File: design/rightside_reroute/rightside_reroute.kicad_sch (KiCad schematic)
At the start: 191 parts, among them IC2 XC9148G50CER-G, IC3 nRF52833-QDAA-R7, IC4 74AHCT125PW,118, IC5 MCP23018T-E_SS, IC6 XC9291B33D1R-G, J1 USB_C_Receptacle_USB2.0_16P, J2 Battery Pos, J3 Battery Neg, J4 OLED_128x32, J6 Conn_01x04, J7 F32Q-1A7H1-11012, U2 BQ24072RGT, U3 USB6B1, U4 BQ27441-G1, U5 PEC11L-4015F-S0015, U6 PEC11L-4015F-S0015, Y1 ECS-320-8-37B2-JTY-TR

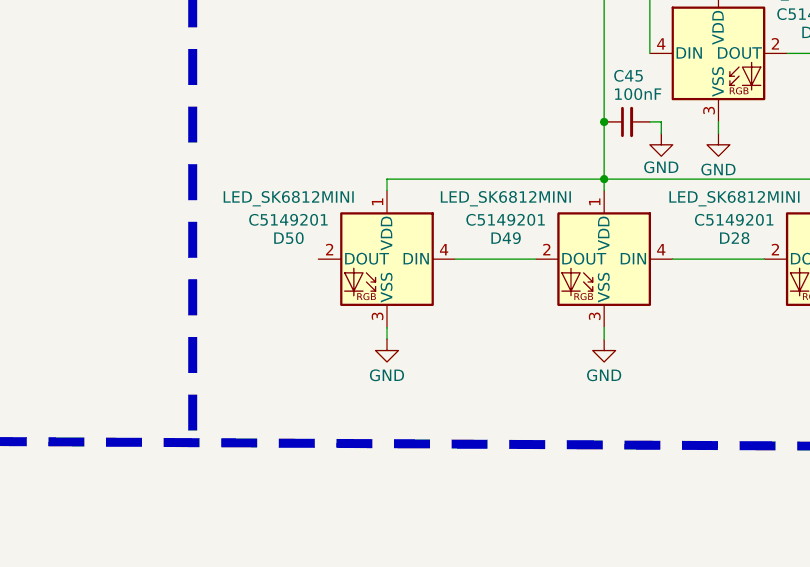
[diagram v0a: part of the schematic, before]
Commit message: reroute power input
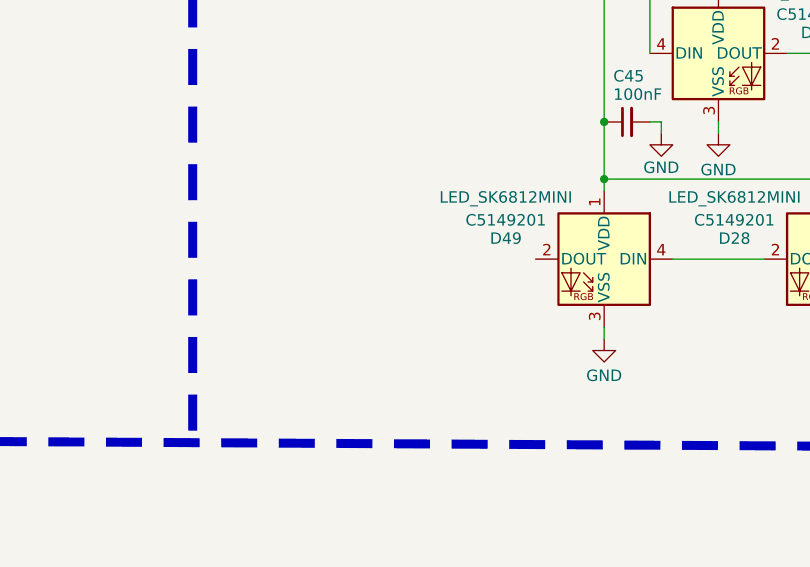
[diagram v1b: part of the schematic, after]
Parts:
- removed D50: LED_SK6812MINI, ScottoKeebs_Components:LED_SK6812MINI, symbol ScottoKeebs:LED_SK6812MINI
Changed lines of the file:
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@@
 	(wire
 		(pts
-			(xy 387.35 229.87) (xy 387.35 231.14)
-		)
-		(stroke
-			(width 0)
-			(type default)
-		)
-	)
-	(wire
-		(pts
 			(xy 508 50.8) (xy 518.16 50.8)
 		)
@@
 	(wire
 		(pts
-			(xy 387.35 213.36) (xy 387.35 214.63)
-		)
-		(stroke
-			(width 0)
-			(type default)
-		)
-	)
-	(wire
-		(pts
 			(xy 372.11 41.91) (xy 424.18 41.91)
 		)
@@
 	(wire
 		(pts
-			(xy 394.97 222.25) (xy 403.86 222.25)
-		)
-		(stroke
-			(width 0)
-			(type default)
-		)
-	)
-	(wire
-		(pts
 			(xy 266.7 203.2) (xy 267.97 203.2)
 		)
@@
 	(wire
 		(pts
-			(xy 411.48 213.36) (xy 387.35 213.36)
-		)
-		(stroke
-			(width 0)
-			(type default)
-		)
-	)
-	(wire
-		(pts
 			(xy 551.18 208.28) (xy 551.18 207.01)
 		)
@@
 	)
 	(symbol
-		(lib_id "power:GND")
-		(at 387.35 231.14 0)
-		(mirror y)
-		(unit 1)
-		(exclude_from_sim no)
-		(in_bom yes)
-		(on_board yes)
-		(dnp no)
-		(property "Reference" "#PWR0110"
-			(at 387.35 237.49 0)
-			(effects
-				(font
-					(size 1.27 1.27)
-				)
-				(hide yes)
-			)
-		)
-		(property "Value" "GND"
-			(at 387.35 235.204 0)
-			(effects
-				(font
-					(size 1.27 1.27)
-				)
-			)
-		)
-		(property "Footprint" ""
-			(at 387.35 231.14 0)
-			(effects
-				(font
-					(size 1.27 1.27)
-				)
-				(hide yes)
-			)
-		)
-		(property "Datasheet" ""
-			(at 387.35 231.14 0)
-			(effects
-				(font
-					(size 1.27 1.27)
-				)
-				(hide yes)
-			)
-		)
-		(property "Description" "Power symbol creates a global label with name \"GND\" , ground"
-			(at 387.35 231.14 0)
-			(effects
-				(font
-					(size 1.27 1.27)
-				)
-				(hide yes)
-			)
-		)
-		(pin "1"
-		)
-		(instances
-			(project "rightside_reroute"
-				(path "/0454547d-f090-46a4-b0ab-f58aec48f156"
-					(reference "#PWR0110")
-					(unit 1)
-				)
-			)
-		)
-	)
-	(symbol
 		(lib_id "ScottoKeebs:Placeholder_Keyswitch")
 		(at 57.15 261.62 0)
@@
 					(unit 1)
 				)
-			)
-		)
-	)
-	(symbol
-		(lib_id "ScottoKeebs:LED_SK6812MINI")
-		(at 387.35 222.25 0)
-		(mirror y)
-		(unit 1)
-		(exclude_from_sim no)
-		(in_bom yes)
-		(on_board yes)
-		(dnp no)
-		(property "Reference" "D50"
-			(at 376.428 219.964 0)
-			(effects
-				(font
-					(size 1.27 1.27)
-				)
-			)
-		)
-		(property "Value" "LED_SK6812MINI"
-			(at 376.428 215.392 0)
-			(effects
-				(font
-					(size 1.27 1.27)
-				)
-			)
-		)
-		(property "Footprint" "ScottoKeebs_Components:LED_SK6812MINI"
-			(at 386.08 229.87 0)
-			(effects
-				(font
-					(size 1.27 1.27)
-				)
-				(justify left top)
-				(hide yes)
-			)
-		)
-		(property "Datasheet" "https://cdn-shop.adafruit.com/product-files/2686/SK6812MINI_REV.01-1-2.pdf"
-			(at 386.08 233.426 0)
-			(effects
-				(font
-					(size 1.27 1.27)
-				)
-				(justify left top)
-				(hide yes)
-			)
-		)
-		(property "Description" "RGB LED with integrated controller"
-			(at 369.062 232.41 0)
-			(effects
-				(font
-					(size 1.27 1.27)
-				)
-				(hide yes)
-			)
-		)
-		(property "LCSC" "C5149201"
-			(at 376.428 217.932 0)
-			(effects
-				(font
-					(size 1.27 1.27)
-				)
-			)
-		)
-		(pin "4"
-		)
-		(pin "3"
-		)
-		(pin "1"
-		)
-		(pin "2"
-		)
-		(instances
-			(project "rightside_reroute"
-				(path "/0454547d-f090-46a4-b0ab-f58aec48f156"
-					(reference "D50")
-					(unit 1)
-				)

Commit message: rerouting 3v3 transformer
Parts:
- removed D49: LED_SK6812MINI, ScottoKeebs_Components:LED_SK6812MINI, symbol ScottoKeebs:LED_SK6812MINI
- removed U4: BQ27441-G1, Package_SON:Texas_S-PDSO-N12, symbol Battery_Management:BQ27441-G1
- added 5V_5: TestPoint, TestPoint:TestPoint_Pad_D1.5mm, symbol Connector:TestPoint
- added C46: 100nF, ScottoKeebs_Components:Capacitor_0603, symbol Device:C_Small
- added IC1: BQ27441DRZT-G1A, SON40P400X250X100-13N-D, symbol SamacSys_Parts:BQ27441DRZT-G1A
- renumbered D29 to D26, D33 to D27, D37 to D28, D41 to D29, D45 to D30, D47 to D31, D43 to D32, D39 to D33, D35 to D34, D31 to D35, D27 to D36, D26 to D37, D30 to D38, D34 to D39, D38 to D40, D42 to D41, D46 to D42, D48 to D43, D40 to D45, D36 to D46, D32 to D47, D28 to D48
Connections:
- net 3V3: no longer C40.2
- net 5V: now also C40.2, 5V_5.1, C46.2
- net BAT: now also IC1.6 (BAT), IC1.8 (SRP)
- net BAT_SRN: now also IC1.7 (SRN)
- net GND: now also R7.1, U6.MH1, U6.MH2, C46.1, IC1.13 (THERMAL_PAD), IC1.3 (VSS); no longer R7.2
- net SCL: now also IC1.2 (SCL)
- net SDA: now also IC1.1 (SDA)
- net VDD: now reaches R8.1
- net VDD: now also C22.1, IC1.5 (VDD)
- net at R8.2: now also IC1.12 (GPOUT); no longer C22.1
- new net: IC1.10 (BIN), R7.2
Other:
- moved on the sheet: BAT_1, C18, C22, R6, R7, R8

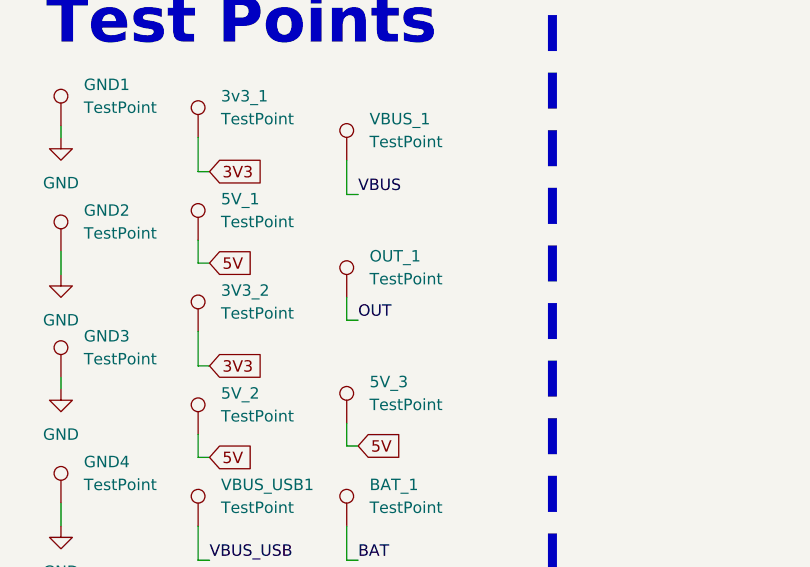
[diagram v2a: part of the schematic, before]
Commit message: prepare to correct bq27441
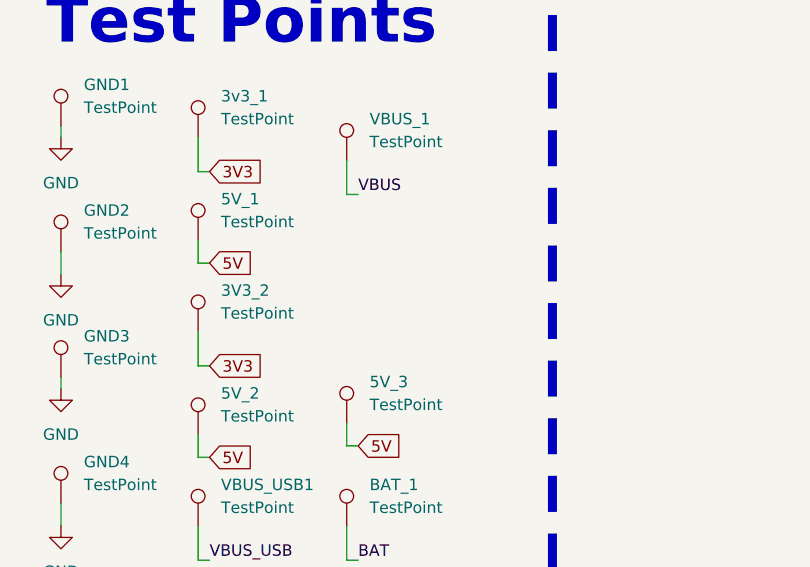
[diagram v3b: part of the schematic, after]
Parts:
- removed OUT_1: TestPoint, TestPoint:TestPoint_Pad_D1.5mm, symbol Connector:TestPoint
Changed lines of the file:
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@@
 	(wire
 		(pts
-			(xy 215.9 281.94) (xy 217.17 281.94)
-		)
-		(stroke
-			(width 0)
-			(type default)
-		)
-	)
-	(wire
-		(pts
 			(xy 82.55 107.95) (xy 101.6 107.95)
 		)
@@
 	(wire
 		(pts
-			(xy 215.9 279.4) (xy 215.9 281.94)
-		)
-		(stroke
-			(width 0)
-			(type default)
-		)
-	)
-	(wire
-		(pts
 			(xy 199.39 318.77) (xy 199.39 322.58)
 		)
@@
 		)
 	)
-	(label "OUT"
-		(at 217.17 281.94 0)
-		(fields_autoplaced yes)
-		(effects
-			(font
-				(size 1.27 1.27)
-			)
-			(justify left bottom)
-		)
-	)
 	(label "Column 5"
 		(at 74.93 73.66 0)
@@
 					(unit 1)
 				)
-			)
-		)
-	)
-	(symbol
-		(lib_id "Connector:TestPoint")
-		(at 215.9 279.4 0)
-		(unit 1)
-		(exclude_from_sim no)
-		(in_bom yes)
-		(on_board yes)
-		(dnp no)
-		(fields_autoplaced yes)
-		(property "Reference" "OUT_1"
-			(at 218.44 274.8279 0)
-			(effects
-				(font
-					(size 1.27 1.27)
-				)
-				(justify left)
-			)
-		)
-		(property "Value" "TestPoint"
-			(at 218.44 277.3679 0)
-			(effects
-				(font
-					(size 1.27 1.27)
-				)
-				(justify left)
-			)
-		)
-		(property "Footprint" "TestPoint:TestPoint_Pad_D1.5mm"
-			(at 220.98 279.4 0)
-			(effects
-				(font
-					(size 1.27 1.27)
-				)
-				(hide yes)
-			)
-		)
-		(property "Datasheet" "~"
-			(at 220.98 279.4 0)
-			(effects
-				(font
-					(size 1.27 1.27)
-				)
-				(hide yes)
-			)
-		)
-		(property "Description" "test point"
-			(at 215.9 279.4 0)
-			(effects
-				(font
-					(size 1.27 1.27)
-				)
-				(hide yes)
-			)
-		)
-		(pin "1"
-		)
-		(instances
-			(project "design_schematic"
-				(path "/0454547d-f090-46a4-b0ab-f58aec48f156"
-					(reference "OUT_1")
-					(unit 1)
-				)

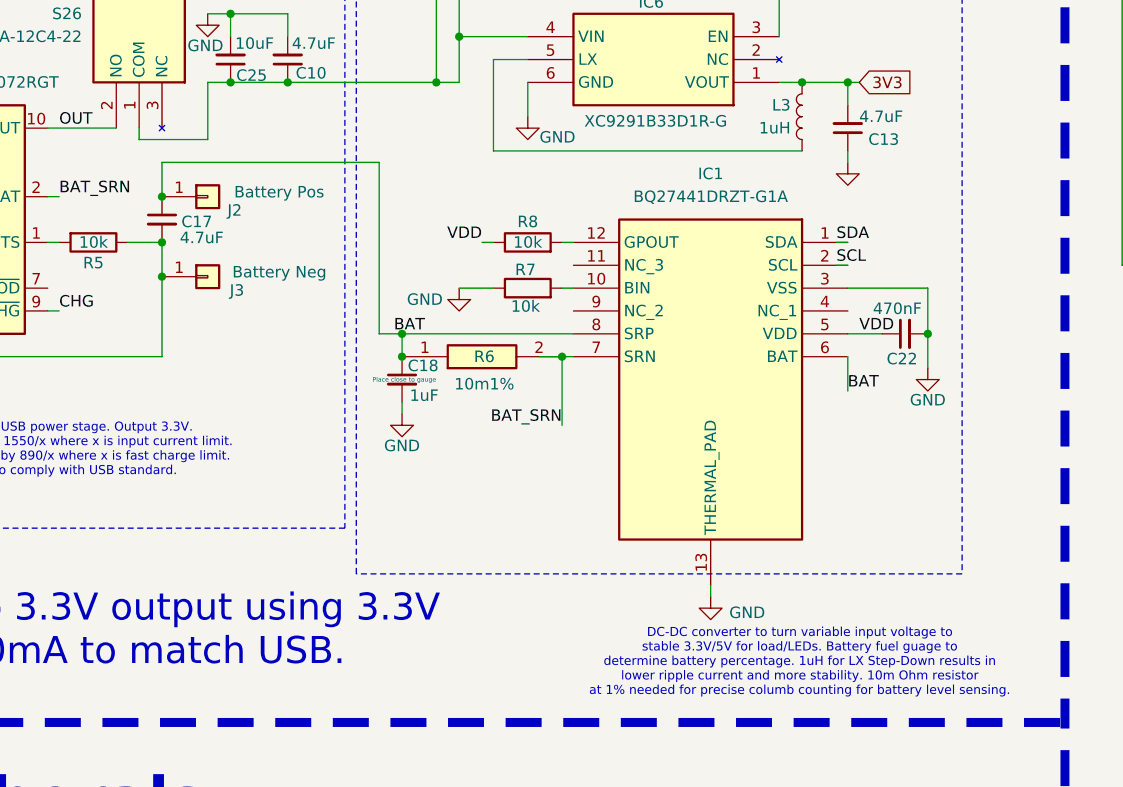
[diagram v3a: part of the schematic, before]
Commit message: right side backlight complete
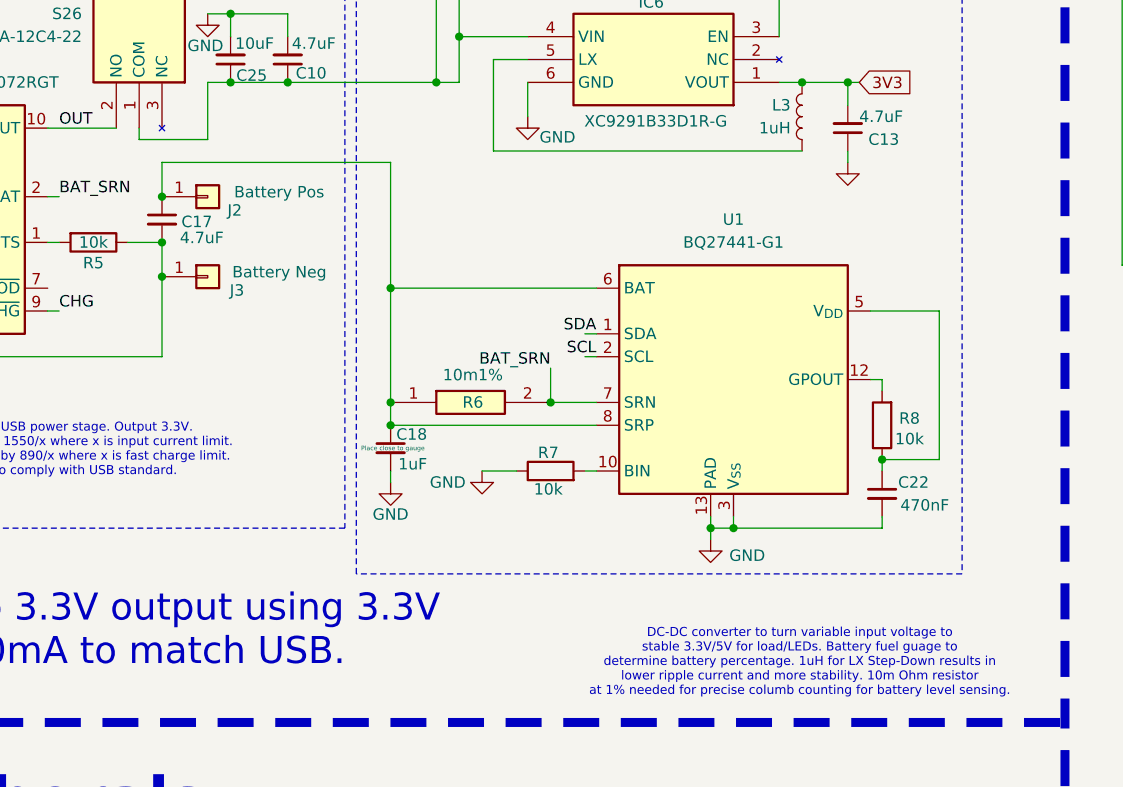
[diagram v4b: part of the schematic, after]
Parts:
- removed IC1: BQ27441DRZT-G1A, SON40P400X250X100-13N-D, symbol SamacSys_Parts:BQ27441DRZT-G1A
- added U1: BQ27441-G1, Package_SON:Texas_S-PDSO-N12, symbol Battery_Management:BQ27441-G1
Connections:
- net BAT: no longer C17.1, C18.1, J2.1 (Pin_1), R6.1
- net BAT_SRN: now also U1.7 (SRN)
- net GND: now also U1.13 (PAD), U1.3 (V_{SS})
- net SCL: now also U1.2 (SCL)
- net SDA: now also U1.1 (SDA)
- net at R7.2: now also U1.10 (BIN)
- net at R8.2: now also U1.12 (GPOUT)
- net VDD: no longer names the net of C22.1, R8.1
- net VDD: now also U1.5 (V_{DD})
- new net: C17.1, C18.1, J2.1 (Pin_1), R6.1, U1.6 (BAT), U1.8 (SRP)
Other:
- moved on the sheet: C18, C22, R6, R7, R8
